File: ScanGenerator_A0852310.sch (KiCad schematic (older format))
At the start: 0 parts

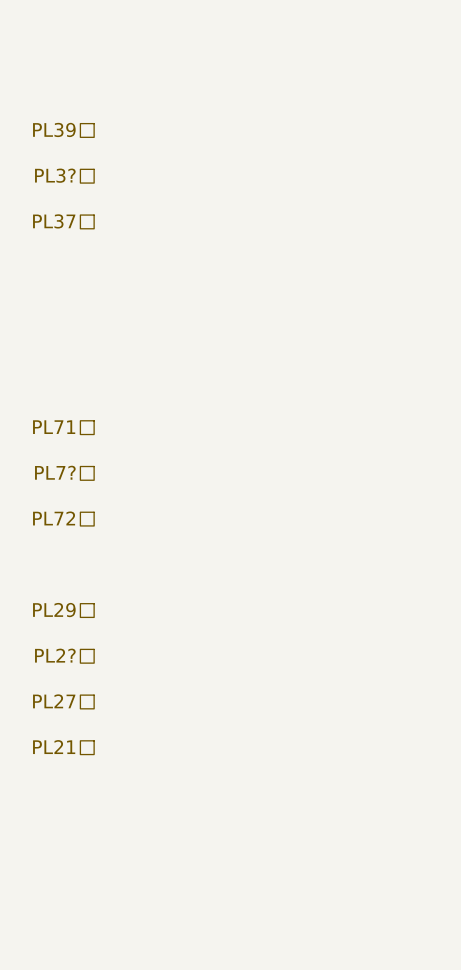
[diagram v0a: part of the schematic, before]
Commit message: Corrects mistakes in existing sub schematics
This corrections were done based on comparison with the actual paper
schematics.
Mainly renaming some pins, which were labled wrongly, plus addid of additional
pins (sockets) which had been overlooked.
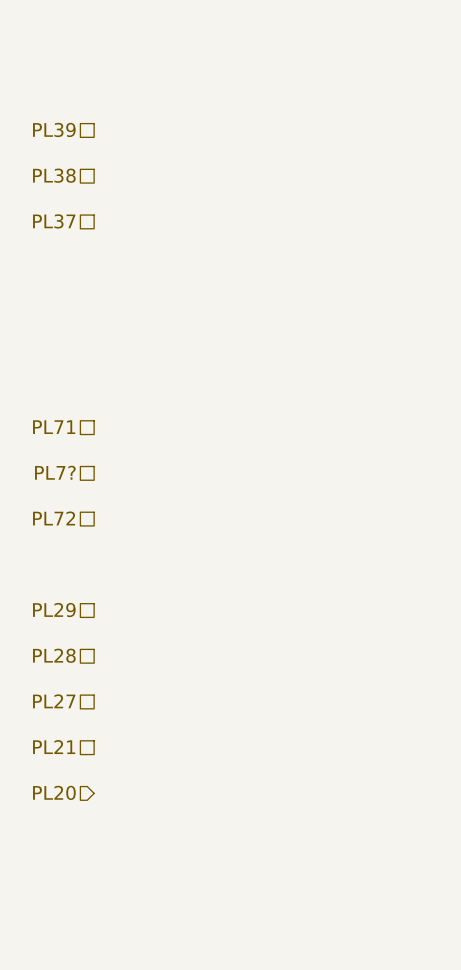
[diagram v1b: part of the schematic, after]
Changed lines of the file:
@@
 LIBS:contrib
 LIBS:valves
+LIBS:Stereoscan120-cache
 EELAYER 26 0
 EELAYER END
 $Descr A4 11693 8268
 encoding utf-8
-Sheet 7 11
+Sheet 7 12
 Title ""
 Date ""
@@
 $EndDescr
 Text HLabel 1500 1700 0    60   UnSpc ~ 0
-PL3?
+PL38
 Text HLabel 1500 1900 0    60   UnSpc ~ 0
 PL37
@@
 PL72
 Text HLabel 1500 3800 0    60   UnSpc ~ 0
-PL2?
+PL28
 Text HLabel 1500 4000 0    60   UnSpc ~ 0
 PL27
@@
 Text HLabel 4000 1000 1    60   UnSpc ~ 0
 PL16
+Text HLabel 1500 4400 0    60   Input ~ 0
+PL20
 $EndSCHEMATC
